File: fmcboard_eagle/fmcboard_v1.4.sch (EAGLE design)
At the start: 160 parts, among them IC1 OPA699ID, IC10 LTC6229IMS8E#TRPBF, IC11 7805TV, IC12 SN74AUC2G66DCTR, IC13 SN74AUC2G66DCTR, IC14 SN74AUC2G66DCTR, IC15 SN74AUC2G66DCTR, IC16 DAC7578SPWR, IC2 DAC7578SPWR, IC3 LTC6229IMS8E#TRPBF, IC4 LTC6229IMS8E#TRPBF, IC5 LM358, IC6 OPA699ID, IC7 OPA699ID, IC8 LTC6229IMS8E#TRPBF, IC9 LTC6229IMS8E#TRPBF, J1 8pin, J10 8pin, J12 4p-2.54, J2 ASP-134604-01, J3 4p-2.54, J4 4p-2.54, J5 8pin, J6 4p-2.54, J7 4p-2.54, J8 4p-2.54, J9 8pin, U1 TXS0108EPWR, U2 STMICROELECTRONICS_L7905ACVST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

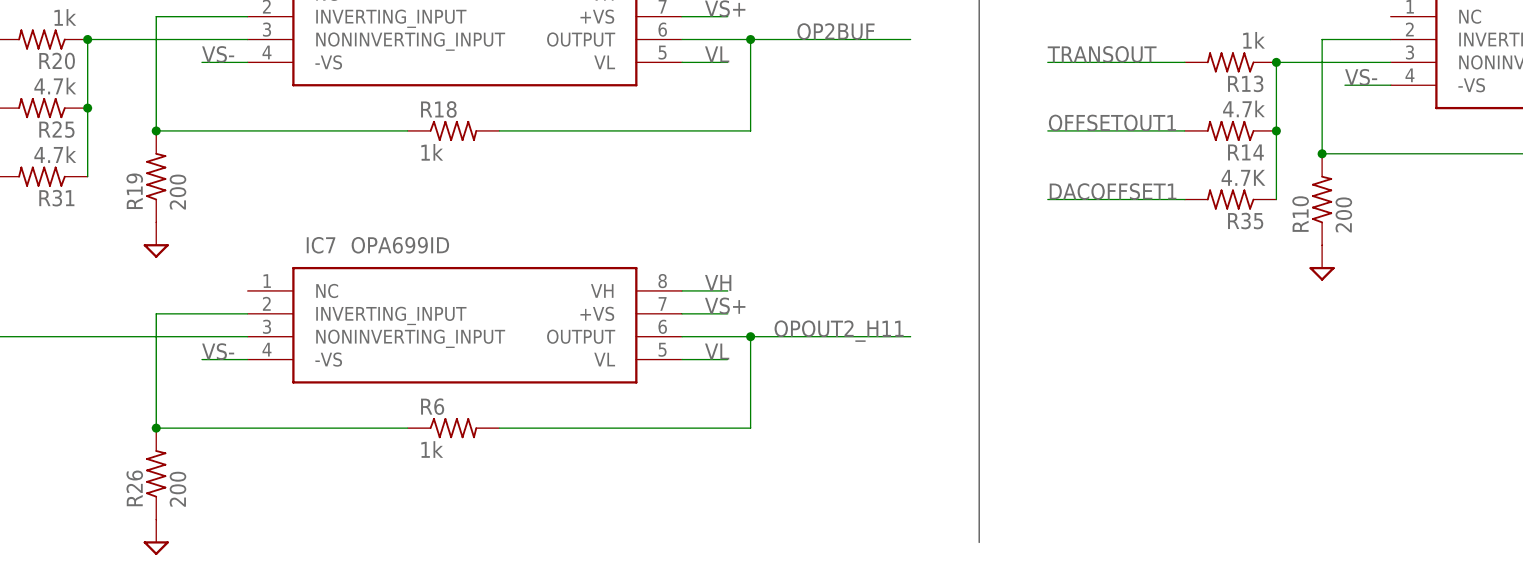
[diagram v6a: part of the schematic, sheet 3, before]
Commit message: Gain resistors updated to 1k, 100
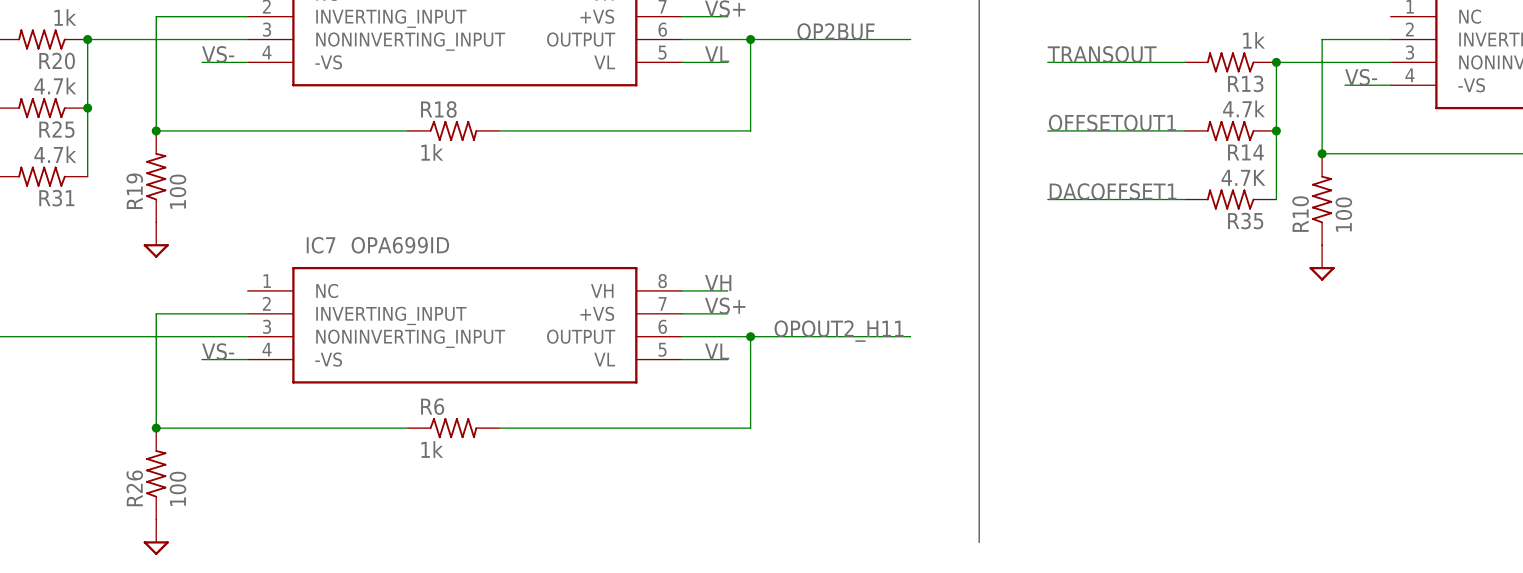
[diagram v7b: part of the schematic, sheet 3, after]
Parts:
- R10, R19, R26: value 200 -> 100
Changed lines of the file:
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@@
 <part name="ARDUINO_NANO1" library="ArduinoNanoV30" deviceset="ARDUINO_NANO" device="" value="1"/>
 <part name="R9" library="rcl" library_urn="urn:adsk.eagle:library:334" deviceset="R-US_" device="R0805" package3d_urn="urn:adsk.eagle:package:23553/2" value="1k"/>
-<part name="R10" library="rcl" library_urn="urn:adsk.eagle:library:334" deviceset="R-US_" device="R0805" package3d_urn="urn:adsk.eagle:package:23553/2" value="200"/>
+<part name="R10" library="rcl" library_urn="urn:adsk.eagle:library:334" deviceset="R-US_" device="R0805" package3d_urn="urn:adsk.eagle:package:23553/2" value="100"/>
 <part name="R13" library="rcl" library_urn="urn:adsk.eagle:library:334" deviceset="R-US_" device="R0805" package3d_urn="urn:adsk.eagle:package:23553/2" value="1k"/>
 <part name="R14" library="rcl" library_urn="urn:adsk.eagle:library:334" deviceset="R-US_" device="R0805" package3d_urn="urn:adsk.eagle:package:23553/2" value="4.7k"/>
@@
 <part name="SUPPLY29" library="supply2" library_urn="urn:adsk.eagle:library:372" deviceset="GND" device=""/>
 <part name="R18" library="rcl" library_urn="urn:adsk.eagle:library:334" deviceset="R-US_" device="R0805" package3d_urn="urn:adsk.eagle:package:23553/2" value="1k"/>
-<part name="R19" library="rcl" library_urn="urn:adsk.eagle:library:334" deviceset="R-US_" device="R0805" package3d_urn="urn:adsk.eagle:package:23553/2" value="200"/>
+<part name="R19" library="rcl" library_urn="urn:adsk.eagle:library:334" deviceset="R-US_" device="R0805" package3d_urn="urn:adsk.eagle:package:23553/2" value="100"/>
 <part name="R20" library="rcl" library_urn="urn:adsk.eagle:library:334" deviceset="R-US_" device="R0805" package3d_urn="urn:adsk.eagle:package:23553/2" value="1k"/>
 <part name="R25" library="rcl" library_urn="urn:adsk.eagle:library:334" deviceset="R-US_" device="R0805" package3d_urn="urn:adsk.eagle:package:23553/2" value="4.7k"/>
@@
 <part name="SUPPLY19" library="supply2" library_urn="urn:adsk.eagle:library:372" deviceset="GND" device=""/>
 <part name="R6" library="rcl" library_urn="urn:adsk.eagle:library:334" deviceset="R-US_" device="R0805" package3d_urn="urn:adsk.eagle:package:23553/2" value="1k"/>
-<part name="R26" library="rcl" library_urn="urn:adsk.eagle:library:334" deviceset="R-US_" device="R0805" package3d_urn="urn:adsk.eagle:package:23553/2" value="200"/>
+<part name="R26" library="rcl" library_urn="urn:adsk.eagle:library:334" deviceset="R-US_" device="R0805" package3d_urn="urn:adsk.eagle:package:23553/2" value="100"/>
 <part name="SUPPLY33" library="supply2" library_urn="urn:adsk.eagle:library:372" deviceset="GND" device=""/>
 <part name="R27" library="rcl" library_urn="urn:adsk.eagle:library:334" deviceset="R-US_" device="R0805" package3d_urn="urn:adsk.eagle:package:23553/2" value="100"/>
